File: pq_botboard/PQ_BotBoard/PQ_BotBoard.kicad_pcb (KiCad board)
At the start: 6 copper layers, 64 x 52 mm, 28 parts, among them IC1 TCN75AVOA713, J1 53261-1471, J2 Conn_01x08_MountingPin, J3 53261-0271

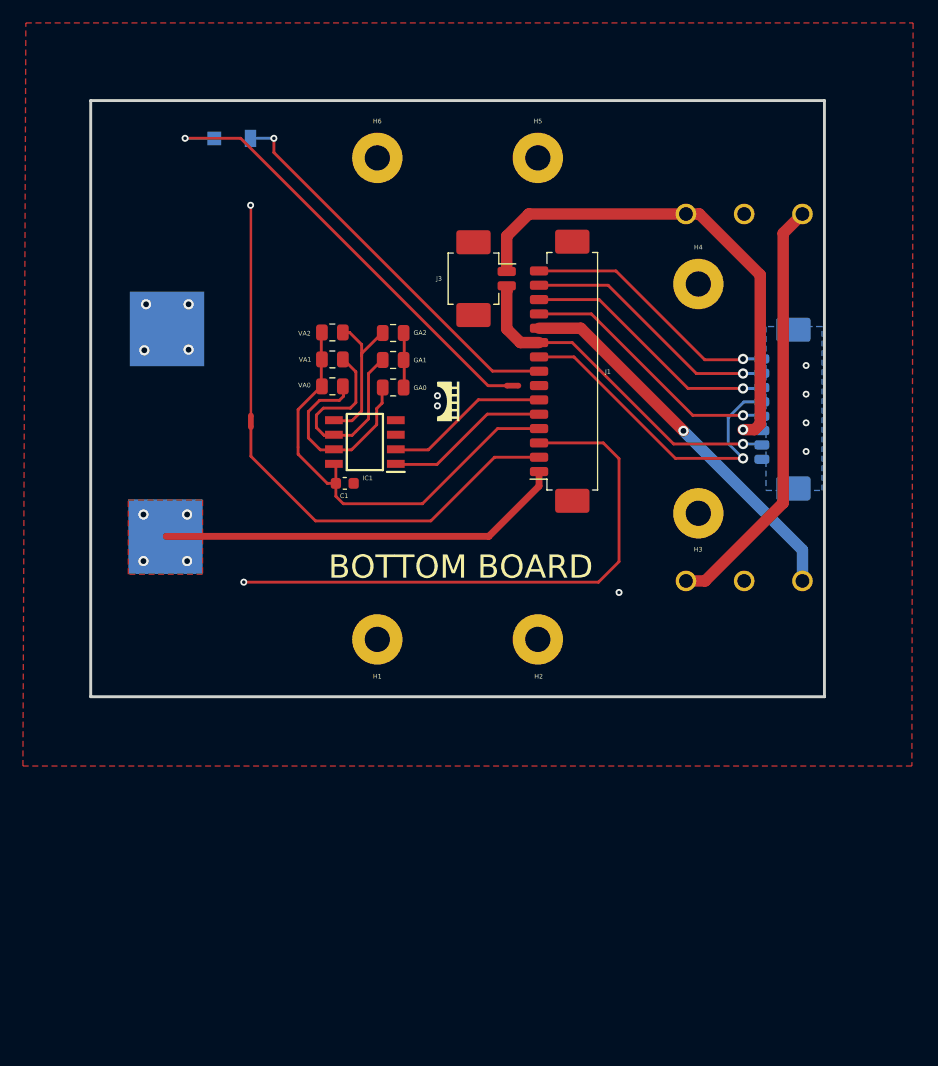
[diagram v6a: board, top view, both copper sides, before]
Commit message: Updated outer boards design as required by the change from Azur Space house-cut solar cells to Lighttricity's S3040_CIC model. Preserved the older design in lat_board_old
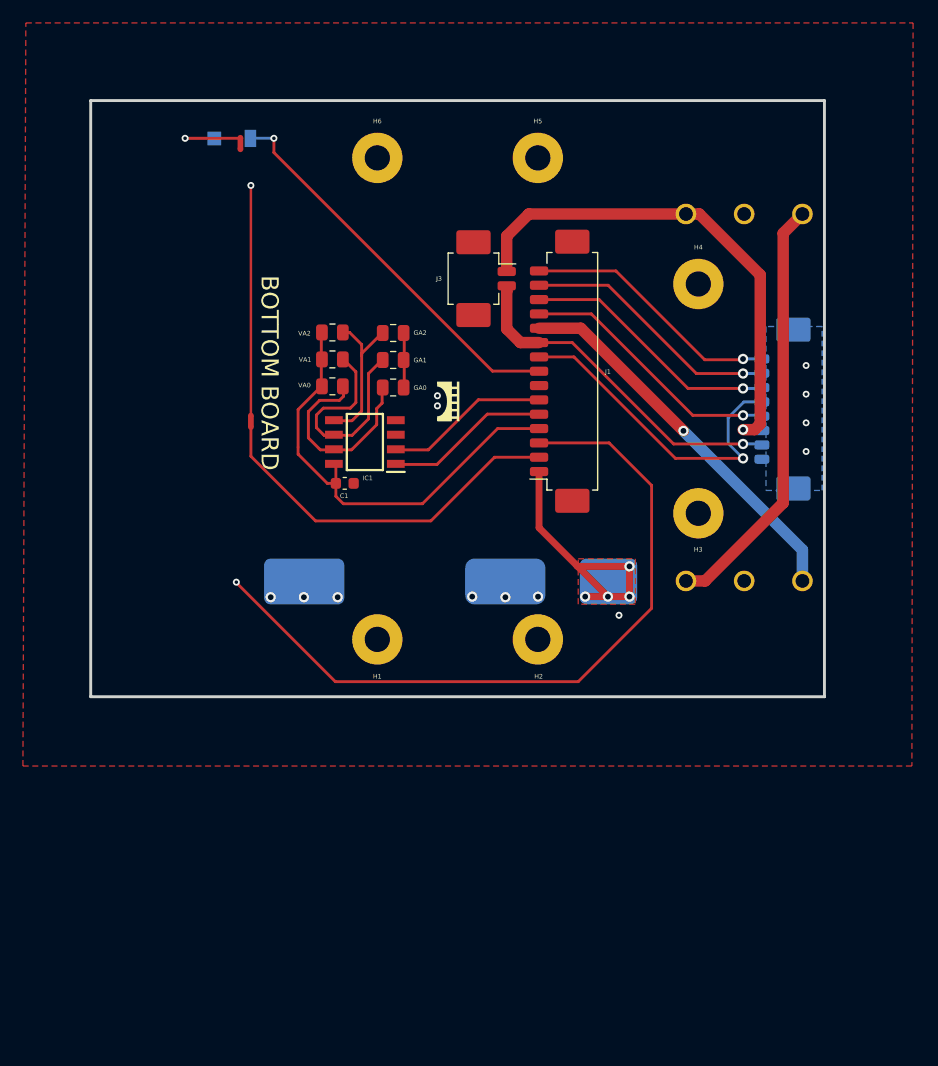
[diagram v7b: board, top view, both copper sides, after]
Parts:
- SC1: value Solar_Cell -> ~; footprint -nsl_power:Azur-Space-PQ-cut-SC -> power-nsl:Lighttricity_S3040_CIC
- moved NT2 31.8 mm to (83.1, 34.7), turned to -90 degrees
- moved SC1 25.6 mm to (77.5, 69.9), turned to 0 degrees
- moved Annotation1 4.93 mm to (74.0, 64.9)
- moved Annotation2 3.74 mm to (73.6, 43.6)
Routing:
- net /PH-: track 39.6 -> 7.41 mm
- net /VCC_MAG: track 9704.1 -> 9726.7 mm
- net /SOLAR_Y: track 35.6 -> 24.5 mm
- net GND: track 4.82 -> 4.75 mm, vias 8 -> 10
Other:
- board text added: "D1"
